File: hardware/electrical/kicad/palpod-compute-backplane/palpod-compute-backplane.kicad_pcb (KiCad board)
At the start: 14 copper layers, 450 x 300 mm, 6 parts

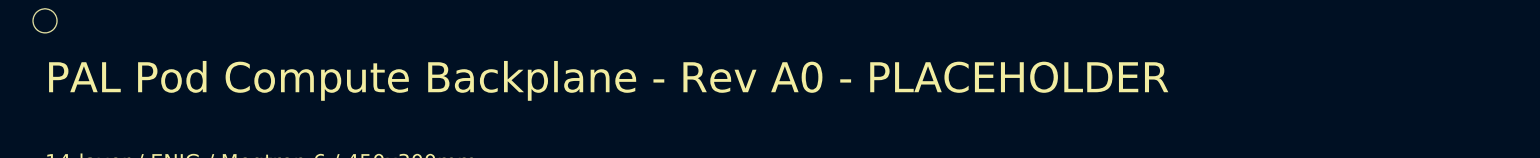
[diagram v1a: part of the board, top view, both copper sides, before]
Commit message: brand: broad KiCad sweep — remaining PAL Pod strings → Hearth
Targeted-pattern sed in ff14a48 missed variants. Broad find-replace
on .kicad_sch/pcb/pro/sym/mod + fp-lib-table + sym-lib-table +
per-project README.md (only where PAL Pod string actually appeared).
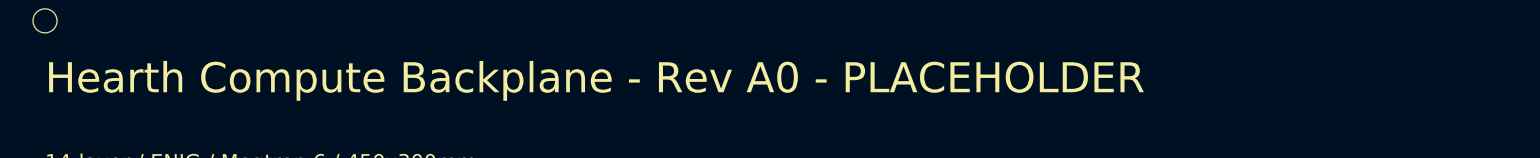
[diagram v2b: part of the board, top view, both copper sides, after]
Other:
- board text added: "Hearth Compute Backplane - Rev A0 - PLACEHOLDER"
- board text removed: "PAL Pod Compute Backplane - Rev A0 - PLACEHOLDER"
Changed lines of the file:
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@@
   (paper "A2")
   (title_block
-    (title "PAL Pod Compute Backplane - PCB")
+    (title "Hearth Compute Backplane - PCB")
     (date "2026-08-03")
     (rev "A0")
@@
     (pad "1" np_thru_hole circle (at 0 0) (size 3.2 3.2) (drill 3.2) (layers "F&B.Cu" "*.Mask"))
   )
-  (gr_text "PAL Pod Compute Backplane - Rev A0 - PLACEHOLDER" (at 225 20 0) (layer "F.SilkS") (effects (font (size 4 4) (thickness 0.6)) (justify left bottom)))
+  (gr_text "Hearth Compute Backplane - Rev A0 - PLACEHOLDER" (at 225 20 0) (layer "F.SilkS") (effects (font (size 4 4) (thickness 0.6)) (justify left bottom)))
   (gr_text "14-layer / ENIG / Megtron 6 / 450x300mm" (at 225 30 0) (layer "F.SilkS") (effects (font (size 2 2) (thickness 0.3)) (justify left bottom)))
   (gr_text "See block-diagrams/compute-backplane.md for topology" (at 225 280 0) (layer "F.SilkS") (effects (font (size 1.5 1.5) (thickness 0.2)) (justify left bottom)))
